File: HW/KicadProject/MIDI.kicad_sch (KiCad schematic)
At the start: 4 parts, among them J2 Conn_01x03, U1 74LVC1G34

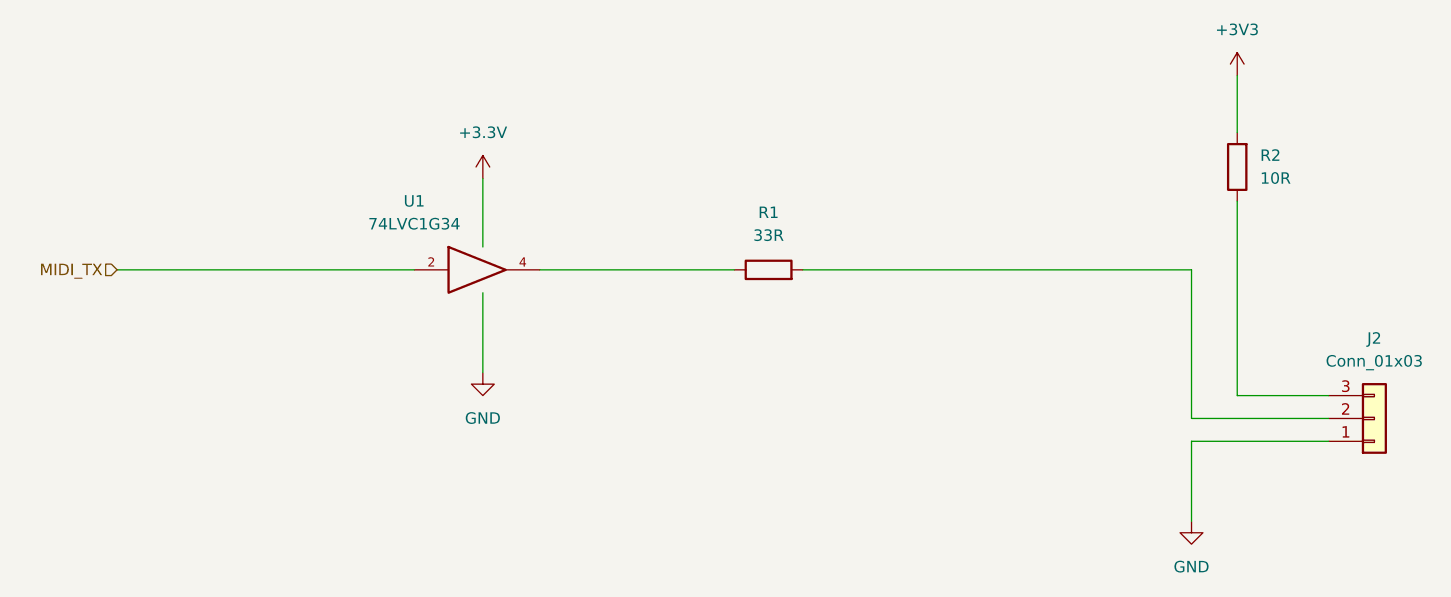
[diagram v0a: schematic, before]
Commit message: Updated to kicad 7.0.1, added stm32 doc links into schema page, regen pdf schema
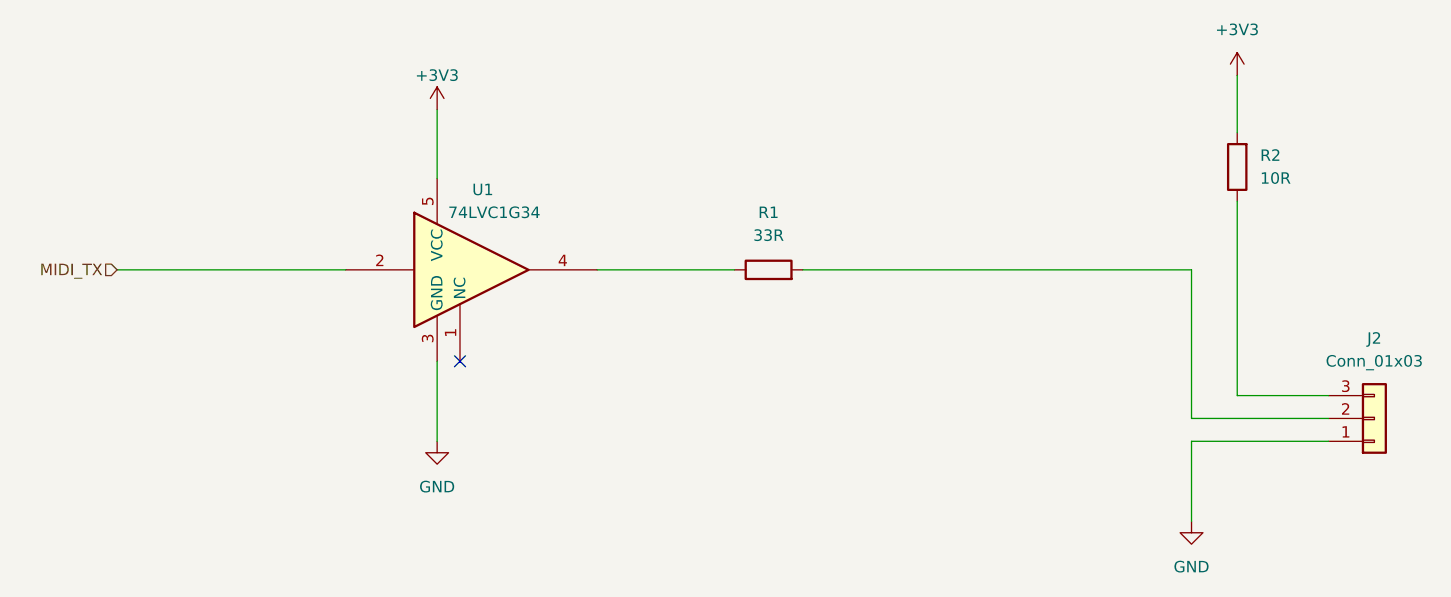
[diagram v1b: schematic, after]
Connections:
- no-connect marks 0 -> 1
